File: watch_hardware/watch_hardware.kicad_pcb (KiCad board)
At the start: 4 copper layers, 31.5 x 39 mm, 58 parts, among them J1 USB_C_Receptacle_USB2.0_16P, Q1 NMOS, Q2 NMOS, SW1 TS24CA_250gf_013, SW2 TS24CA_250gf_013, SW3 TS24CA_250gf_013, SW4 TS24CA_250gf_013, U1 ESP32-S3-PICO-1-N8R8, U2 LIS3MDL, U3 LSM6DSOW, U4 TK018F3716, U5 TPS62825DMQR, U6 TP4057, U7 ICS-43434

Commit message: 基本重新设计了硬件部分
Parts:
- removed C19: 100nF, Capacitor_SMD:C_0402_1005Metric
- removed Q2: NMOS, Package_TO_SOT_SMD:SOT-23
- removed R20: 100k, Resistor_SMD:R_0402_1005Metric_Pad0.72x0.64mm_HandSolder
- removed U7: ICS-43434, projects:MIC-SMD_6P-L3.5-W2.7-P0.90-BL
- removed test1, test2: NC, Resistor_SMD:R_0402_1005Metric_Pad0.72x0.64mm_HandSolder
- added C20: 10uF, Capacitor_SMD:C_0402_1005Metric, F.Cu at (149.7, 55.9)
- added D1: B5819WS, Diode_SMD:D_SOD-323, F.Cu at (144.8, 56.0)
- added F1: Fuse_Small, Fuse:Fuse_0402_1005Metric, F.Cu at (155.0, 93.2)
- added R21: 10k, Resistor_SMD:R_0402_1005Metric_Pad0.72x0.64mm_HandSolder, F.Cu at (181.0, 73.8)
- added U8: AW9523B, Package_DFN_QFN:QFN-24-1EP_4x4mm_P0.5mm_EP2.7x2.7mm, F.Cu at (162.1, 66.5)
- C3: value 100nF -> 10uF
- R1: value 10k -> 4.7k
- R10: value 10k -> 680k
- U1: value ESP32-S3-PICO-1-N8R8 -> ESP32-S3-PICO-1-N8R2
- moved Q1 61.4 mm to (133.3, 78.3)
- moved R14 61.4 mm to (130.7, 77.7)
- moved R15 61.4 mm to (131.3, 75.8)
- moved R16 61.4 mm to (133.7, 75.8)
- moved BT1 57.9 mm to (159.5, 46.4)
- moved C18 50.4 mm to (147.2, 90.4)
- moved C8 50.4 mm to (144.7, 93.8)
- moved C9 50.4 mm to (143.6, 93.8)
- moved L1 50.4 mm to (146.6, 93.3)
- moved R17 50.4 mm to (147.2, 91.5)
- moved U5 50.4 mm to (149.9, 93.3), turned to 180 degrees
- moved C10 50.4 mm to (152.8, 93.2)
- moved R18 50.4 mm to (144.8, 91.5)
- moved R8 50.4 mm to (151.8, 93.2)
- moved R1 47.6 mm to (146.4, 55.9), turned to 90 degrees
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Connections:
- BT1 pad 1: /BAT -> Net-(BT1-+)
- C3 pad 1: Net-(U1-CHIP_PU) -> GND
- C3 pad 2: GND -> Net-(U1-CHIP_PU)
- C5 pad 1: /GPIO2 -> /GPIO0
- C6 pad 1: /GPIO3 -> /GPIO2
- C7 pad 1: /GPIO4 -> /GPIO3
- Q1 pad 2: Net-(Q1-G) -> /ADC_P
- R1 pad 1: +3V3 -> Net-(U1-CHIP_PU)
- R1 pad 2: Net-(U1-CHIP_PU) -> Net-(D1A-K)
- R10 pad 1: Net-(U1-GPIO0) -> Net-(U1-CHIP_PU)
- R10 pad 2: +3V3 -> GND
- R14 pad 1: Net-(U1-GPIO7) -> Net-(U1-GPIO6)
- R15 pad 1: Net-(U1-GPIO7) -> Net-(U1-GPIO6)
- R16 pad 1: Net-(Q1-G) -> /ADC_P
- R19 pad 1: /CHRG -> +3V3
- R19 pad 2: +3V3 -> /CHRG
- R5 pad 1: /GPIO2 -> /GPIO0
- R6 pad 1: /GPIO3 -> /GPIO2
- R7 pad 1: /GPIO4 -> /GPIO3
- SW2 pad 1: /GPIO2 -> /GPIO0
- SW3 pad 1: /GPIO3 -> /GPIO2
- SW4 pad 1: /GPIO4 -> /GPIO3
- U1 pad 10: /SDA0 -> /SCL0
- U1 pad 11: /SCL0 -> Net-(U1-GPIO6)
- U1 pad 12: Net-(U1-GPIO7) -> unconnected-(U1-GPIO7-Pad12)
- U1 pad 13: Net-(Q1-G) -> unconnected-(U1-GPIO8-Pad13)
- U1 pad 14: /CHRG -> unconnected-(U1-GPIO9-Pad14)
- U1 pad 23: /L_RST -> /L_TE
- U1 pad 24: /L_TE -> unconnected-(U1-GPIO18-Pad24)
- U1 pad 5: Net-(U1-GPIO0) -> /GPIO0
- U1 pad 51: /LCD_L -> unconnected-(U1-GPIO45-Pad51)
- U1 pad 9: /GPIO4 -> /SDA0
- U4 pad 21: /L_RST -> /T_RST
- U6 pad 5: unconnected-(U6-STDBY-Pad5) -> /STDBY
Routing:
- net +3V3: track 176.3 -> 19.1 mm, vias 14 -> 2
- net /SDA0: track 53.3 -> 0.00 mm, vias 4 -> 0
- net /SCL0: track 50.4 -> 0.00 mm, vias 3 -> 0
- net /LCD_L: track 49.8 -> 0.00 mm, vias 2 -> 0
- net /GPIO4: track 42.6 -> 0.00 mm, vias 1 -> 0
- net /GPIO3: track 40.0 -> 0.00 mm, vias 1 -> 0
- net /CHRG: track 28.2 -> 0.00 mm, vias 2 -> 0
- net /BAT: track 26.6 -> 0.00 mm
- net GND: track 25.6 -> 0.00 mm, vias 70 -> 0
- net /SCK: track 22.9 -> 0.00 mm
- net /GPIO0: track 0.00 -> 21.4 mm, vias 0 -> 1
- net /GPIO2: track 21.1 -> 0.00 mm, vias 1 -> 0
- net /USB_D+: track 20.9 -> 0.00 mm, vias 1 -> 0
- net /L_CS: track 19.4 -> 0.00 mm, vias 2 -> 0
- net /SD: track 18.9 -> 0.00 mm
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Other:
- board size 31.5 x 39 mm -> 31.7 x 39.6 mm
- board text removed: "R 0"

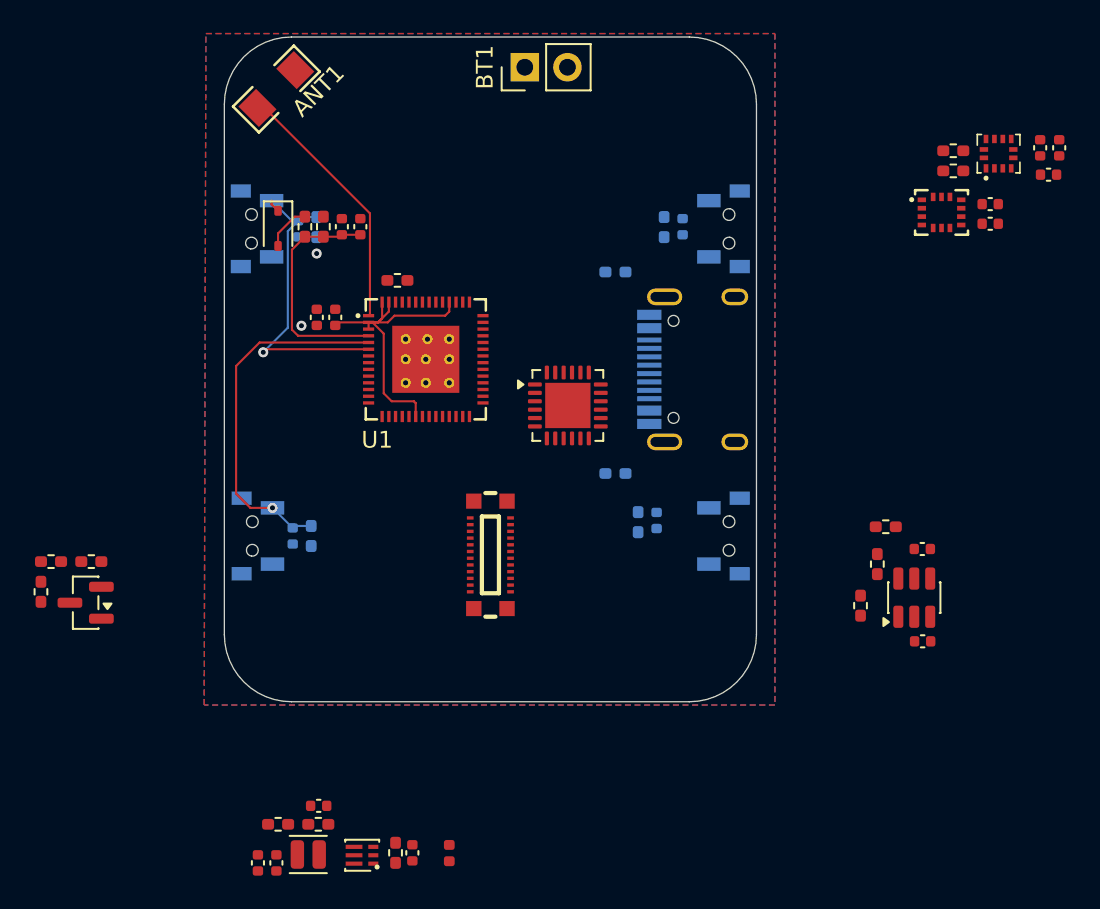
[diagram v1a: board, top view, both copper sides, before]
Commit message: 修改了电路部分，使用外部flash
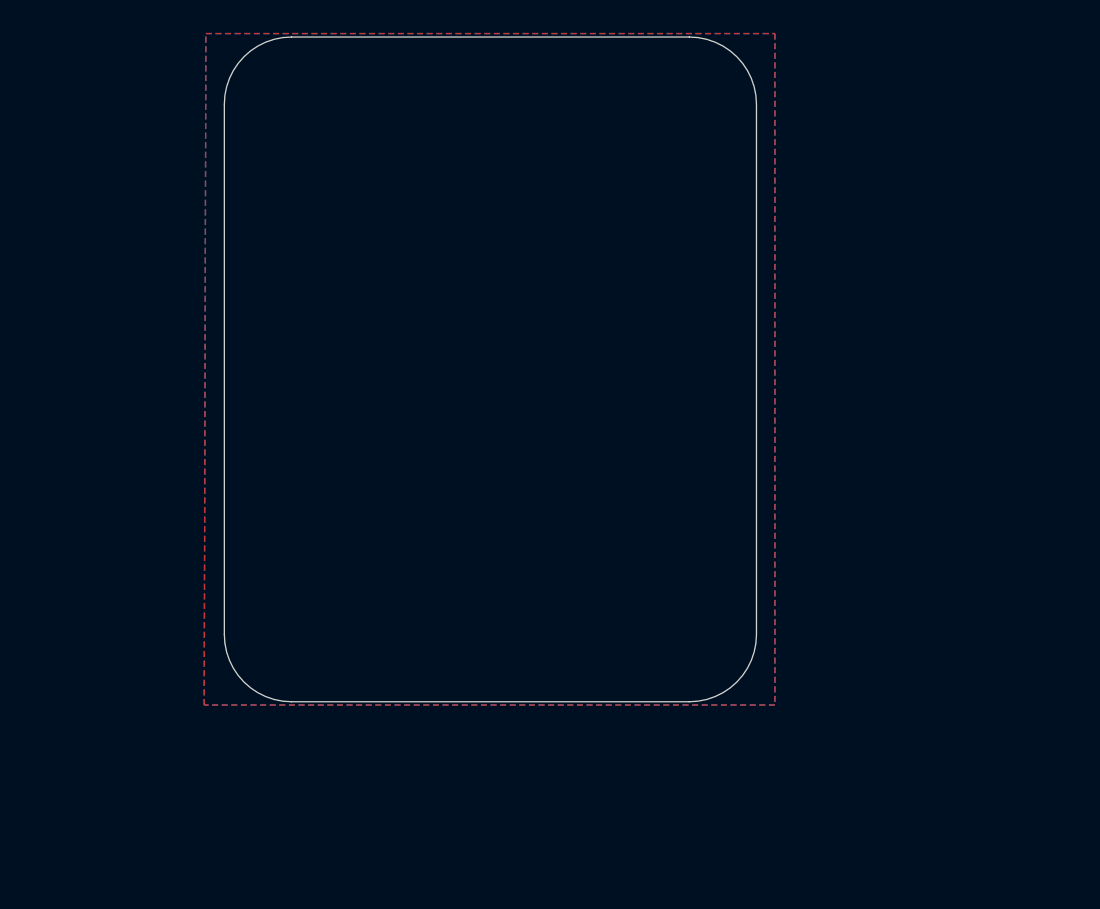
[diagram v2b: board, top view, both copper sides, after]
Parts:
- removed ANT1: ANT-SMD-2_L3.2-W1.6, projects:ANT-SMD-2_L3.2-W1.6
- removed BT1: Battery_Cell, Connector_PinHeader_2.54mm:PinHeader_1x02_P2.54mm_Vertical
- removed C1, C11, C12, C13, C15, C20, C3, C8, C9: 10uF, Capacitor_SMD:C_0402_1005Metric
- removed C10: 4.7uF, Capacitor_SMD:C_0402_1005Metric
- removed C14, C16, C17, C2, C4, C5, C6, C7: 100nF, Capacitor_SMD:C_0402_1005Metric
- removed C18: 120pF, Capacitor_SMD:C_0402_1005Metric
- removed D1: B5819WS, Diode_SMD:D_SOD-323
- removed F1: Fuse_Small, Fuse:Fuse_0402_1005Metric
- removed J1: USB_C_Receptacle_USB2.0_16P, Connector_USB:USB_C_Receptacle_HRO_TYPE-C-31-M-12
- removed L1: 1uH, Inductor_SMD:L_Changjiang_FTC201610S
- removed Q1: NMOS, Package_TO_SOT_SMD:SOT-23
- removed R1, R12, R13: 4.7k, Resistor_SMD:R_0402_1005Metric_Pad0.72x0.64mm_HandSolder
- removed R10: 680k, Resistor_SMD:R_0402_1005Metric_Pad0.72x0.64mm_HandSolder
- removed R11, R15, R16, R19, R21, R4, R5, R6, R7: 10k, Resistor_SMD:R_0402_1005Metric_Pad0.72x0.64mm_HandSolder
- removed R14: 20k, Resistor_SMD:R_0402_1005Metric_Pad0.72x0.64mm_HandSolder
- removed R17: 68k, Resistor_SMD:R_0402_1005Metric_Pad0.72x0.64mm_HandSolder
- removed R18: 15k, Resistor_SMD:R_0402_1005Metric_Pad0.72x0.64mm_HandSolder
- removed R2, R3: 5.1k, Resistor_SMD:R_0402_1005Metric_Pad0.72x0.64mm_HandSolder
- removed R8: 100k, Resistor_SMD:R_0402_1005Metric_Pad0.72x0.64mm_HandSolder
- removed R9: 6.8k, Resistor_SMD:R_0402_1005Metric_Pad0.72x0.64mm_HandSolder
- removed SW1, SW2, SW3, SW4: TS24CA_250gf_013, projects:SW-SMD_L4.7-W3.5-P3.35-EH
- removed U1: ESP32-S3-PICO-1-N8R2, esp32-s3-pico-1:QFN-56_L7.0-W7.0-P0.40-TL-EP4.0
- removed U2: LIS3MDL, projects:LGA-12_L2.0-W2.0-P0.50-BL
- removed U3: LSM6DSOW, projects:LGA-14L_L3.0-W2.5-P0.50-TL
- removed U4: TK018F3716, projects:CONN-SMD_BTB0.408-24PLBDR-M41
- removed U5: TPS62825DMQR, projects:QFN-6_1.55x1.55_Pitch0.4mm
- removed U6: TP4057, Package_TO_SOT_SMD:TSOT-23-6
- removed U8: AW9523B, Package_DFN_QFN:QFN-24-1EP_4x4mm_P0.5mm_EP2.7x2.7mm
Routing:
- net /GPIO0: track 21.4 -> 0.00 mm, vias 1 -> 0
- net +3V3: track 19.1 -> 0.00 mm, vias 2 -> 0
- net /GPIO1: track 19.1 -> 0.00 mm, vias 1 -> 0
- net Net-(ANT1-INPUT): track 15.4 -> 0.00 mm
- net Net-(U1-CHIP_PU): track 13.9 -> 0.00 mm
- net Net-(D1A-K): track 2.76 -> 0.00 mm

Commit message: 简单的画了了一下PCB
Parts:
- added ANT1: ANT-SMD-2_L3.2-W1.6, projects:ANT-SMD-2_L3.2-W1.6, F.Cu at (144.7, 81.0)
- added BT1: Battery_Cell, Connector_PinHeader_2.54mm:PinHeader_1x02_P2.54mm_Vertical, F.Cu at (149.5, 46.4)
- added C1: 100nF, Capacitor_SMD:C_0402_1005Metric, F.Cu at (114.0, 43.5)
- added C10: 18pF, Capacitor_SMD:C_0402_1005Metric, F.Cu at (152.7, 57.0)
- added C11: 10uF, Capacitor_SMD:C_0603_1608Metric, F.Cu at (170.8, 76.4)
- added C12: 100nF, Capacitor_SMD:C_0402_1005Metric, F.Cu at (170.5, 75.0)
- added C13: 100nF, Capacitor_SMD:C_0402_1005Metric, F.Cu at (116.9, 43.5)
- added C14: 100nF, Capacitor_SMD:C_0402_1005Metric, F.Cu at (116.9, 45.5)
- added C15: 10uF, Capacitor_SMD:C_0603_1608Metric, F.Cu at (113.8, 70.7)
- added C16: 10uF, Capacitor_SMD:C_0603_1608Metric, F.Cu at (113.8, 72.5)
- added C17: 100nF, Capacitor_SMD:C_0402_1005Metric, F.Cu at (116.9, 47.4)
- added C18: 10uF, Capacitor_SMD:C_0603_1608Metric, F.Cu at (113.8, 74.2)
- added C19: 4.7uF, Capacitor_SMD:C_0402_1005Metric, F.Cu at (116.9, 49.4)
- added C2: 100nF, Capacitor_SMD:C_0402_1005Metric, F.Cu at (114.0, 45.5)
- added C20: 10uF, Capacitor_SMD:C_0603_1608Metric, F.Cu at (113.8, 76.0)
- added C21: 270pF, Capacitor_SMD:C_0402_1005Metric, F.Cu at (116.9, 51.4)
- added C22: 10uF, Capacitor_SMD:C_0603_1608Metric, F.Cu at (116.2, 63.7)
- added C23: 10uF, Capacitor_SMD:C_0603_1608Metric, F.Cu at (116.2, 65.5)
- added C24: 100nF, Capacitor_SMD:C_0402_1005Metric, F.Cu at (116.9, 53.3)
- added C25: 100nF, Capacitor_SMD:C_0402_1005Metric, F.Cu at (116.9, 55.3)
- added C26: 10uF, Capacitor_SMD:C_0603_1608Metric, F.Cu at (116.2, 67.2)
- added C27: 100pF, Capacitor_SMD:C_0402_1005Metric, F.Cu at (116.9, 57.3)
- added C28: 10uF, Capacitor_SMD:C_0603_1608Metric, F.Cu at (116.2, 69.0)
- added C29: 100nF, Capacitor_SMD:C_0402_1005Metric, F.Cu at (119.7, 43.5)
- added C3: 100nF, Capacitor_SMD:C_0402_1005Metric, F.Cu at (114.0, 47.4)
- added C30: 10uF, Capacitor_SMD:C_0603_1608Metric, F.Cu at (150.5, 53.3)
- added C31: 100nF, Capacitor_SMD:C_0402_1005Metric, F.Cu at (152.7, 51.1)
- added C32: 10uF, Capacitor_SMD:C_0603_1608Metric, F.Cu at (116.2, 72.5)
- added C33: 10uF, Capacitor_SMD:C_0603_1608Metric, F.Cu at (156.2, 49.4)
- added C34: 100nF, Capacitor_SMD:C_0402_1005Metric, F.Cu at (143.2, 50.2)
- added C35: 10uF, Capacitor_SMD:C_0603_1608Metric, F.Cu at (157.8, 49.4)
- added C36: 10uF, Capacitor_SMD:C_0603_1608Metric, F.Cu at (157.9, 55.7)
- added C37: 10uF, Capacitor_SMD:C_0603_1608Metric, F.Cu at (154.7, 50.1)
- added C38: 10uF, Capacitor_SMD:C_0603_1608Metric, F.Cu at (153.1, 46.6)
- added C4: 100nF, Capacitor_SMD:C_0402_1005Metric, F.Cu at (114.0, 49.4)
- added C40: 10uF, Capacitor_SMD:C_0603_1608Metric, F.Cu at (157.8, 52.6)
- added C41: 100nF, Capacitor_SMD:C_0402_1005Metric, F.Cu at (156.5, 55.1)
- added C42: 10uF, Capacitor_SMD:C_0603_1608Metric, F.Cu at (154.7, 46.6)
- added C43: 10uF, Capacitor_SMD:C_0603_1608Metric, F.Cu at (156.2, 52.6)
- added C45: 10uF, Capacitor_SMD:C_0603_1608Metric, F.Cu at (118.7, 74.2)
- added C46: 100nF, Capacitor_SMD:C_0402_1005Metric, F.Cu at (119.7, 55.3)
- added C47: 1uF, Capacitor_SMD:C_0402_1005Metric, F.Cu at (163.9, 47.0)
- added C48: 100nF, Capacitor_SMD:C_0402_1005Metric, F.Cu at (164.3, 54.8)
- added C49: 10uF, Capacitor_SMD:C_0603_1608Metric, F.Cu at (163.8, 56.1)
- added C5: 10uF, Capacitor_SMD:C_0603_1608Metric, F.Cu at (113.8, 63.7)
- added C51: 10uF, Capacitor_SMD:C_0603_1608Metric, F.Cu at (169.3, 47.4)
- added C52: 10uF, Capacitor_SMD:C_0603_1608Metric, F.Cu at (170.9, 47.4)
- added C53: 100nF, Capacitor_SMD:C_0402_1005Metric, F.Cu at (166.4, 54.8)
- added C54: 10uF, Capacitor_SMD:C_0603_1608Metric, F.Cu at (166.9, 56.1)
- added C55: 100nF, Capacitor_SMD:C_0402_1005Metric, F.Cu at (169.5, 55.2)
- added C56: 10uF, Capacitor_SMD:C_0603_1608Metric, F.Cu at (170.0, 53.8)
- added C6: 100nF, Capacitor_SMD:C_0402_1005Metric, F.Cu at (114.0, 51.4)
- added C7: 10uF, Capacitor_SMD:C_0603_1608Metric, F.Cu at (113.8, 65.5)
- added C8: 10uF, Capacitor_SMD:C_0603_1608Metric, F.Cu at (113.8, 67.2)
- added C9: 18pF, Capacitor_SMD:C_0402_1005Metric, F.Cu at (148.5, 57.0)
- added D1: TVS, Resistor_SMD:R_0402_1005Metric, F.Cu at (106.7, 83.4)
- added D10: D_TVS, Diode_SMD:D_0201_0603Metric, F.Cu at (125.5, 55.6)
- added D11: D_TVS, Diode_SMD:D_0201_0603Metric, F.Cu at (125.5, 57.4)
- added D2: B5819WS, Diode_SMD:D_SOD-323, F.Cu at (136.2, 71.5)
- added D3: D_TVS, Diode_SMD:D_0201_0603Metric, F.Cu at (125.5, 43.4)
- added D4: D_TVS, Diode_SMD:D_0201_0603Metric, F.Cu at (125.5, 45.1)
- added D5: D_TVS, Diode_SMD:D_0201_0603Metric, F.Cu at (125.5, 46.9)
- added D6: D_TVS, Diode_SMD:D_0201_0603Metric, F.Cu at (125.5, 48.6)
- added D7: D_TVS, Diode_SMD:D_0201_0603Metric, F.Cu at (125.5, 50.4)
- added D8: D_TVS, Diode_SMD:D_0201_0603Metric, F.Cu at (125.5, 52.1)
- added D9: D_TVS, Diode_SMD:D_0201_0603Metric, F.Cu at (125.5, 53.9)
- added J1: USB_C_Receptacle_USB2.0_16P, Connector_USB:USB_C_Receptacle_HRO_TYPE-C-31-M-12, F.Cu at (170.8, 65.1)
- added J2: TF_Card, projects:TF-SMD_TF-PUSH, B.Cu at (151.5, 64.2)
- added L1: 4.7uH, Inductor_SMD:L_Changjiang_FTC201610S, F.Cu at (152.4, 49.4)
- added L2: 2.2uH, Inductor_SMD:L_Changjiang_FTC201610S, F.Cu at (160.1, 49.1)
- added L3: 2.2uH, Inductor_SMD:L_Changjiang_FTC201610S, F.Cu at (160.1, 52.4)
- added L4: 2.2uH, Inductor_SMD:L_Changjiang_FTC201610S, F.Cu at (167.1, 46.4)
- added LS1: Speaker, Connector_PinHeader_1.27mm:PinHeader_1x02_P1.27mm_Vertical, F.Cu at (114.6, 59.9)
- added MK1: Microphone, Connector_PinHeader_2.00mm:PinHeader_1x02_P2.00mm_Vertical, F.Cu at (136.0, 51.7)
- added R1: 10k, Resistor_SMD:R_0402_1005Metric_Pad0.72x0.64mm_HandSolder, F.Cu at (95.9, 60.9)
- added R10: 680k, Resistor_SMD:R_0402_1005Metric_Pad0.72x0.64mm_HandSolder, F.Cu at (99.2, 60.9)
- added R11: 4.7k, Resistor_SMD:R_0402_1005Metric_Pad0.72x0.64mm_HandSolder, F.Cu at (99.2, 62.9)
- added R12: 4.7k, Resistor_SMD:R_0402_1005Metric_Pad0.72x0.64mm_HandSolder, F.Cu at (99.2, 64.8)
- added R13: 4.7k, Resistor_SMD:R_0402_1005Metric_Pad0.72x0.64mm_HandSolder, F.Cu at (99.2, 66.8)
- added R14: 4.7k, Resistor_SMD:R_0402_1005Metric_Pad0.72x0.64mm_HandSolder, F.Cu at (99.2, 68.8)
- added R15: 10k, Resistor_SMD:R_0402_1005Metric_Pad0.72x0.64mm_HandSolder, F.Cu at (99.2, 70.8)
- added R16: 10k, Resistor_SMD:R_0402_1005Metric_Pad0.72x0.64mm_HandSolder, F.Cu at (99.2, 72.8)
- added R17: 10k, Resistor_SMD:R_0402_1005Metric_Pad0.72x0.64mm_HandSolder, F.Cu at (99.2, 74.8)
- added R18: 100k, Resistor_SMD:R_0402_1005Metric_Pad0.72x0.64mm_HandSolder, F.Cu at (99.2, 76.8)
- added R19: 82k, Resistor_SMD:R_0402_1005Metric_Pad0.72x0.64mm_HandSolder, F.Cu at (102.5, 60.9)
- added R2: 10k, Resistor_SMD:R_0402_1005Metric_Pad0.72x0.64mm_HandSolder, F.Cu at (95.9, 62.9)
- added R20: 10k, Resistor_SMD:R_0402_1005Metric_Pad0.72x0.64mm_HandSolder, F.Cu at (102.5, 62.9)
- added R21: 8.2k, Resistor_SMD:R_0402_1005Metric_Pad0.72x0.64mm_HandSolder, F.Cu at (102.5, 64.8)
- added R22: 20k, Resistor_SMD:R_0402_1005Metric_Pad0.72x0.64mm_HandSolder, F.Cu at (102.5, 66.8)
- added R23: 22k, Resistor_SMD:R_0402_1005Metric_Pad0.72x0.64mm_HandSolder, F.Cu at (102.5, 68.8)
- added R24: 10k, Resistor_SMD:R_0402_1005Metric_Pad0.72x0.64mm_HandSolder, F.Cu at (102.5, 70.8)
- added R25: 5.6k, Resistor_SMD:R_0402_1005Metric_Pad0.72x0.64mm_HandSolder, B.Cu at (164.1, 61.7)
- added R26: 10k, Resistor_SMD:R_0402_1005Metric_Pad0.72x0.64mm_HandSolder, F.Cu at (102.5, 74.8)
- added R27: 500m, Resistor_SMD:R_0402_1005Metric, F.Cu at (151.8, 46.9)
- added R28: 100k, Resistor_SMD:R_0402_1005Metric_Pad0.72x0.64mm_HandSolder, F.Cu at (156.7, 47.2)
- added R29: 22k, Resistor_SMD:R_0402_1005Metric_Pad0.72x0.64mm_HandSolder, F.Cu at (159.1, 47.2)
- added R3: 10k, Resistor_SMD:R_0402_1005Metric_Pad0.72x0.64mm_HandSolder, F.Cu at (95.9, 64.8)
- added R30: 100k, Resistor_SMD:R_0402_1005Metric_Pad0.72x0.64mm_HandSolder, F.Cu at (172.0, 52.4)
- added R31: 1R0, Resistor_SMD:R_0402_1005Metric_Pad0.72x0.64mm_HandSolder, F.Cu at (163.9, 45.9)
- added R32: 100k, Resistor_SMD:R_0402_1005Metric_Pad0.72x0.64mm_HandSolder, F.Cu at (169.7, 52.4)
- added R33: 100k, Resistor_SMD:R_0402_1005Metric_Pad0.72x0.64mm_HandSolder, F.Cu at (169.7, 49.5)
- added R34: 22k, Resistor_SMD:R_0402_1005Metric_Pad0.72x0.64mm_HandSolder, F.Cu at (169.7, 50.6)
- added R4: 10k, Resistor_SMD:R_0402_1005Metric_Pad0.72x0.64mm_HandSolder, F.Cu at (95.9, 66.8)
- added R5: 5.1k, Resistor_SMD:R_0402_1005Metric_Pad0.72x0.64mm_HandSolder, F.Cu at (95.9, 68.8)
- added R6: 5.1k, Resistor_SMD:R_0402_1005Metric_Pad0.72x0.64mm_HandSolder, F.Cu at (95.9, 70.8)
- added R7: 4.7k, Resistor_SMD:R_0402_1005Metric_Pad0.72x0.64mm_HandSolder, F.Cu at (95.9, 72.8)
- added R8: 200k, Resistor_SMD:R_0402_1005Metric_Pad0.72x0.64mm_HandSolder, F.Cu at (95.9, 74.8)
- added R9: 100k, Resistor_SMD:R_0402_1005Metric_Pad0.72x0.64mm_HandSolder, F.Cu at (95.9, 76.8)
- added SW1: SW_Push, Connector_PinHeader_1.27mm:PinHeader_1x02_P1.27mm_Vertical, F.Cu at (118.8, 59.9)
- added SW2: SW_Push, Connector_PinHeader_1.27mm:PinHeader_1x02_P1.27mm_Vertical, F.Cu at (122.9, 59.9)
- added SW3: SW_Push, Connector_PinHeader_1.27mm:PinHeader_1x02_P1.27mm_Vertical, F.Cu at (127.1, 59.9)
- added SW4: SW_Push, Connector_PinHeader_1.27mm:PinHeader_1x02_P1.27mm_Vertical, F.Cu at (131.2, 59.9)
- added TH1: 10k;B 3950K, Resistor_SMD:R_0402_1005Metric_Pad0.72x0.64mm_HandSolder, B.Cu at (164.1, 60.6)
- added U1: ESP32-S3, Package_DFN_QFN:QFN-56-1EP_7x7mm_P0.4mm_EP5.6x5.6mm, F.Cu at (151.9, 64.4)
- added U10: TP5000, Package_DFN_QFN:QFN-16-1EP_4x4mm_P0.65mm_EP2.5x2.5mm_ThermalVias, F.Cu at (146.4, 51.0)
- added U11: LM2664, Package_TO_SOT_SMD:SOT-23-6, F.Cu at (153.4, 53.4)
- added U12: TPS650250, Package_DFN_QFN:QFN-32-1EP_5x5mm_P0.5mm_EP3.6x3.6mm_ThermalVias, F.Cu at (164.7, 50.7)
- added U2: TK018F3716, projects:CONN-SMD_BTB0.408-24PLBDR-M41, F.Cu at (157.4, 75.5)
- added U3: W25Q128JVP, Package_SON:WSON-8-1EP_6x5mm_P1.27mm_EP3.4x4.3mm, F.Cu at (161.8, 66.4)
- added U4: LIS3MDL, projects:LGA-12_L2.0-W2.0-P0.50-BL, F.Cu at (162.7, 74.1)
- added U5: LSM6DSOW, projects:LGA-14L_L3.0-W2.5-P0.50-TL, F.Cu at (166.9, 73.7)
- added U6: AW9523B, Package_DFN_QFN:QFN-24-1EP_4x4mm_P0.5mm_EP2.7x2.7mm, F.Cu at (150.9, 73.0)
- added U7: LPS22HB, Package_LGA:ST_HLGA-10_2x2mm_P0.5mm_LayoutBorder3x2y, F.Cu at (166.1, 79.5)
- added U8: CJC4344H, Package_SO:MSOP-10_3x3mm_P0.5mm, F.Cu at (182.1, 61.7)
- added U9: OPA2192, Package_SO:VSSOP-8_3x3mm_P0.65mm, F.Cu at (182.2, 67.1)
- added Y1: Crystal_GND24, Crystal:Crystal_SMD_2016-4Pin_2.0x1.6mm, F.Cu at (150.6, 56.9)
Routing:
- net /CS#: track 0.00 -> 16.4 mm, vias 0 -> 2
- net /WP#: track 0.00 -> 16.3 mm, vias 0 -> 2
- net /DI: track 0.00 -> 16.3 mm, vias 0 -> 2
- net /DO: track 0.00 -> 15.5 mm, vias 0 -> 2
- net /VDD_SPI: track 0.00 -> 11.9 mm
- net /SCK: track 0.00 -> 11.8 mm, vias 0 -> 2
- net /HOLD#: track 0.00 -> 11.2 mm
- net Net-(U10-TS): vias 0 -> 2
- net Net-(U1-GPIO46): vias 0 -> 1
- net GND: vias 0 -> 26
- net /TF_DAT3: vias 0 -> 1
- net /TF_DAT2: vias 0 -> 1
- net /TF_DAT1: vias 0 -> 1
- net /TF_DAT0: vias 0 -> 1
- net /TF_CMD: vias 0 -> 1
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
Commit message: 简单天线匹配
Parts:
- added C10: 1pF, Capacitor_SMD:C_0402_1005Metric, F.Cu at (147.3, 59.2)
- added C6: 2.7pF, Capacitor_SMD:C_0402_1005Metric, F.Cu at (144.1, 59.2)
- added L1: 1.5nH, Inductor_SMD:L_0402_1005Metric, F.Cu at (145.7, 59.7)
- added R24: 100, Resistor_SMD:R_0402_1005Metric_Pad0.72x0.64mm_HandSolder, F.Cu at (122.7, 64.2)
- renumbered C9 to C11, C10 to C12, C11 to C13, C12 to C14, C13 to C15, C14 to C16, C15 to C17, C16 to C18, C17 to C19, C18 to C20, C19 to C21, C20 to C22, C21 to C23, C22 to C24, C23 to C25, C24 to C26, C25 to C27, C26 to C28, C27 to C29, C28 to C30, C29 to C31, C30 to C32, C31 to C33, C32 to C34, C34 to C35, C33 to C36, C36 to C37, C37 to C38, C38 to C39, C35 to C40, C40 to C43, C43 to C44, C51 to C50, C52 to C51, C53 to C52, C54 to C53, C55 to C54, C56 to C55, C6 to C7, C7 to C8, C8 to C9, L1 to L2, L2 to L3, L3 to L4, L4 to L5, R24 to R25, R25 to R26, R26 to R27, R27 to R28, R28 to R29, R29 to R30, R30 to R31, R31 to R32, R32 to R33, R33 to R34, R34 to R35
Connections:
- LS1 pad 1: Net-(U9-OUT_B) -> Net-(LS1-Pad1)
- U1 pad 1: Net-(ANT1-INPUT) -> Net-(U1-LNA_IN)
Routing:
- net Net-(ANT1-INPUT): track 0.00 -> 21.7 mm
- net Net-(U1-LNA_IN): track 0.00 -> 3.64 mm
- net GND: vias 26 -> 59

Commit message: daily
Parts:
- D10, D11, D3, D4, D5, D6, D7, D8, D9: moved to B.Cu
- MK1: footprint Connector_PinHeader_2.00mm:PinHeader_1x02_P2.00mm_Vertical -> Connector_PinHeader_1.00mm:PinHeader_1x02_P1.00mm_Vertical
- SW1, SW2, SW3, SW4: footprint Connector_PinHeader_1.27mm:PinHeader_1x02_P1.27mm_Vertical -> Connector_PinHeader_1.00mm:PinHeader_1x02_P1.00mm_Vertical
- moved R4 66.8 mm to (161.3, 80.5)
- moved R3 61.1 mm to (155.1, 79.9), turned to 90 degrees
- moved R2 59.7 mm to (153.1, 79.9), turned to 90 degrees
- moved R1 58.4 mm to (151.1, 79.9), turned to 90 degrees
- moved C4 54.6 mm to (158.9, 80.5)
- moved C3 53.9 mm to (156.6, 80.5)
- moved C2 52.9 mm to (154.1, 80.0), turned to 90 degrees
- moved C1 52.8 mm to (152.1, 80.0), turned to 90 degrees
- moved R7 52.4 mm to (148.1, 77.6), turned to -90 degrees
- moved D3 46.8 mm to (170.0, 58.0), turned to 180 degrees
- moved D4 46.6 mm to (170.0, 58.9), turned to 180 degrees
- moved SW1 39.7 mm to (151.7, 82.1)
- moved MK1 39.6 mm to (161.3, 82.1)
- moved D10 39.0 mm to (160.7, 72.5), turned to 180 degrees
- moved D11 39.0 mm to (160.7, 74.3), turned to 180 degrees
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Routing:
- net /SCK: track 11.8 -> 16.3 mm
- net GND: vias 59 -> 69
